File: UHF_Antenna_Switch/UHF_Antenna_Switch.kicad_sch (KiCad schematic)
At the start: 37 parts, among them J1 Conn_N_Type_Female, J2 Conn_SO-239, J3 Conn_SMA_Female, J4 Screw_Terminal_01x04, J5 Conn_02x03_Odd_Even, SW1 SW_SP3T, SW2 SW_Push, U1 LTC5507ES6, U2 PAT1220-C-10DB, U3 PCB-Trace-RF-Coupler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

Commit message: chore(pcb): Minor layout tweaks in RF area
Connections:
- net RF_PORT_TX: now reaches J2.1 (In), U3.1 (INPUT)
- net Relay_K1/RF_COMMON renamed RF_PORT_ANT
- net Relay_K1/RF_NC renamed RF_PORT_RX
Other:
- moved on the sheet: J2
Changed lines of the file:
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@@
 	)
 	(rectangle
-		(start 27.94 13.97)
+		(start 13.97 13.97)
 		(end 266.7 78.74)
 		(stroke
@@
 	(wire
 		(pts
-			(xy 54.61 45.72) (xy 62.23 45.72)
+			(xy 41.91 45.72) (xy 62.23 45.72)
 		)
 		(stroke
@@
 		)
 	)
+	(label "RF_PORT_RX"
+		(at 156.21 60.96 0)
+		(effects
+			(font
+				(size 1.27 1.27)
+			)
+			(justify left bottom)
+		)
+	)
+	(label "RF_PORT_ANT"
+		(at 222.25 64.77 0)
+		(effects
+			(font
+				(size 1.27 1.27)
+			)
+			(justify left bottom)
+		)
+	)
+	(label "RF_PORT_TX"
+		(at 43.18 45.72 0)
+		(effects
+			(font
+				(size 1.27 1.27)
+			)
+			(justify left bottom)
+		)
+	)
 	(global_label "TX_DETECTED"
 		(shape input)
@@
 	(symbol
 		(lib_id "Connector:Conn_Coaxial")
-		(at 49.53 45.72 0)
+		(at 36.83 45.72 0)
 		(mirror y)
 		(unit 1)
@@
 		(dnp no)
 		(property "Reference" "J2"
-			(at 46.99 44.7431 0)
+			(at 34.29 44.7431 0)
 			(show_name no)
 			(do_not_autoplace no)
@@
 		)
 		(property "Value" "Conn_SO-239"
-			(at 46.99 47.2831 0)
+			(at 34.29 47.2831 0)
 			(show_name no)
 			(do_not_autoplace no)
@@
 		)
 		(property "Footprint" "00-project-footprints:Amphenol N Jack 172234"
-			(at 49.53 45.72 0)
+			(at 36.83 45.72 0)
 			(hide yes)
 			(show_name no)
@@
 		)
 		(property "Datasheet" ""
-			(at 49.53 45.72 0)
+			(at 36.83 45.72 0)
 			(hide yes)
 			(show_name no)
@@
 		)
 		(property "Description" "coaxial connector (BNC, SMA, SMB, SMC, Cinch/RCA, LEMO, ...)"
-			(at 49.53 45.72 0)
+			(at 36.83 45.72 0)
 			(hide yes)
 			(show_name no)
@@
 		)
 		(property "Purpose" "TX/Uplink Input"
-			(at 39.624 49.276 0)
+			(at 26.924 49.276 0)
 			(show_name no)
 			(do_not_autoplace no)
@@
 		)
 		(property "Connector Type" "SO-239 Female"
-			(at 39.116 51.562 0)
+			(at 26.416 51.562 0)
 			(show_name no)
 			(do_not_autoplace no)
@@
 	(symbol
 		(lib_id "power:GNDS")
-		(at 49.53 50.8 0)
+		(at 36.83 50.8 0)
 		(unit 1)
 		(body_style 1)
@@
 		(dnp no)
 		(property "Reference" "#PWR04"
-			(at 49.53 57.15 0)
+			(at 36.83 57.15 0)
 			(hide yes)
 			(show_name no)
@@
 		)
 		(property "Value" "GNDS"
-			(at 49.53 54.864 0)
+			(at 36.83 54.864 0)
 			(show_name no)
 			(do_not_autoplace no)
@@
 		)
 		(property "Footprint" ""
-			(at 49.53 50.8 0)
+			(at 36.83 50.8 0)
 			(hide yes)
 			(show_name no)
@@
 		)
 		(property "Datasheet" ""
-			(at 49.53 50.8 0)
+			(at 36.83 50.8 0)
 			(hide yes)
 			(show_name no)
@@
 		)
 		(property "Description" "Power symbol creates a global label with name \"GNDS\" , signal ground"
-			(at 49.53 50.8 0)
+			(at 36.83 50.8 0)
 			(hide yes)
 			(show_name no)

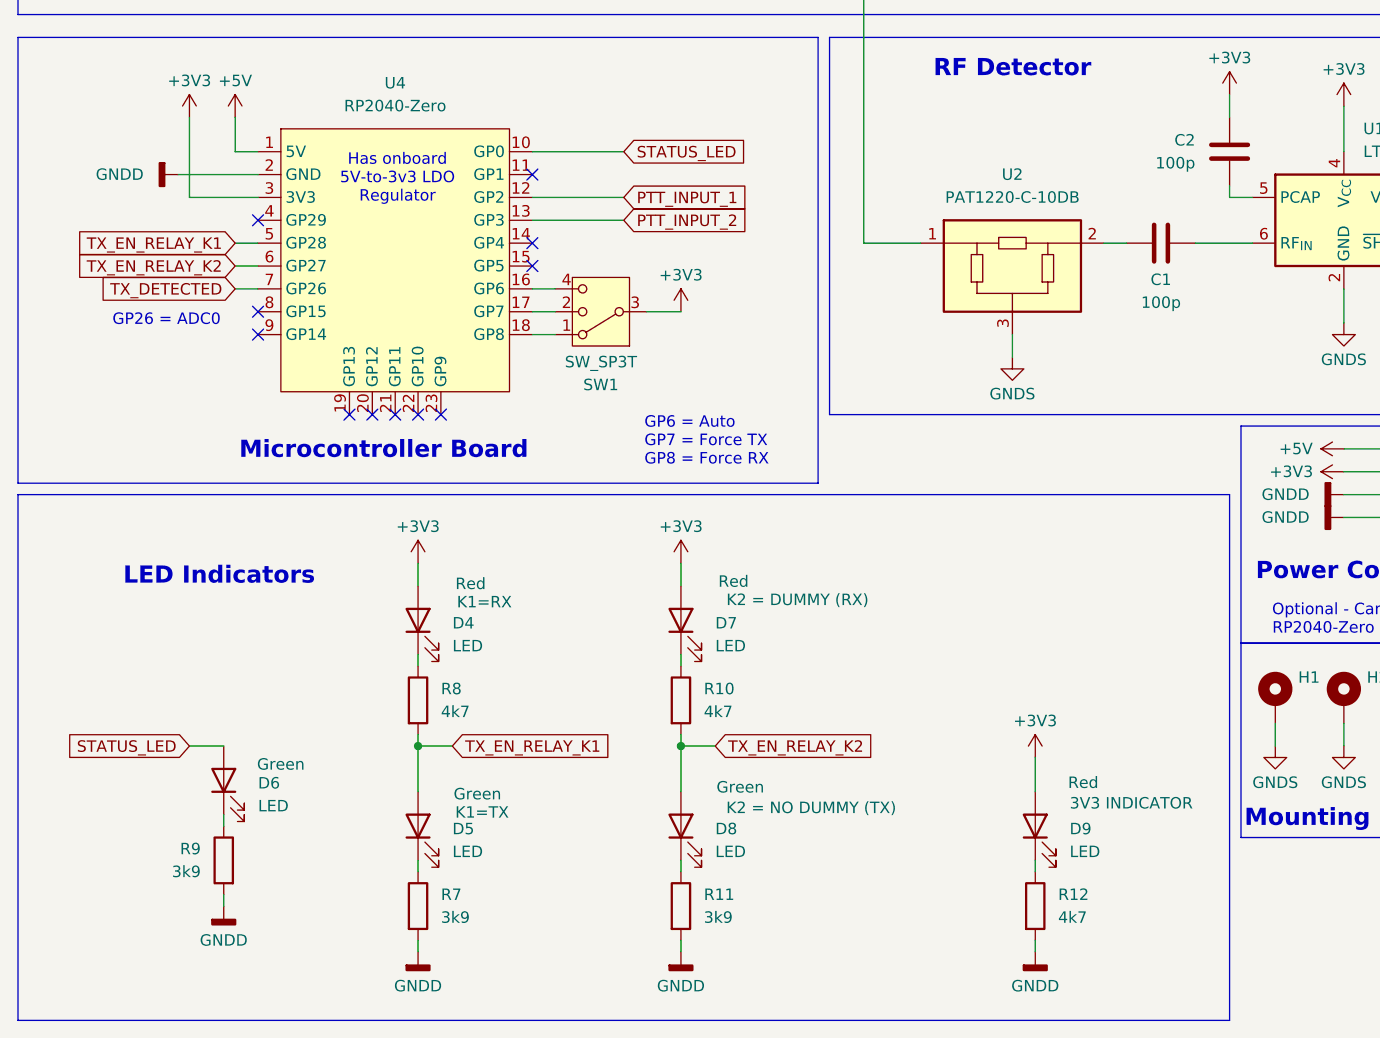
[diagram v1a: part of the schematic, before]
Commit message: feat: Add Serial Override LED indicator
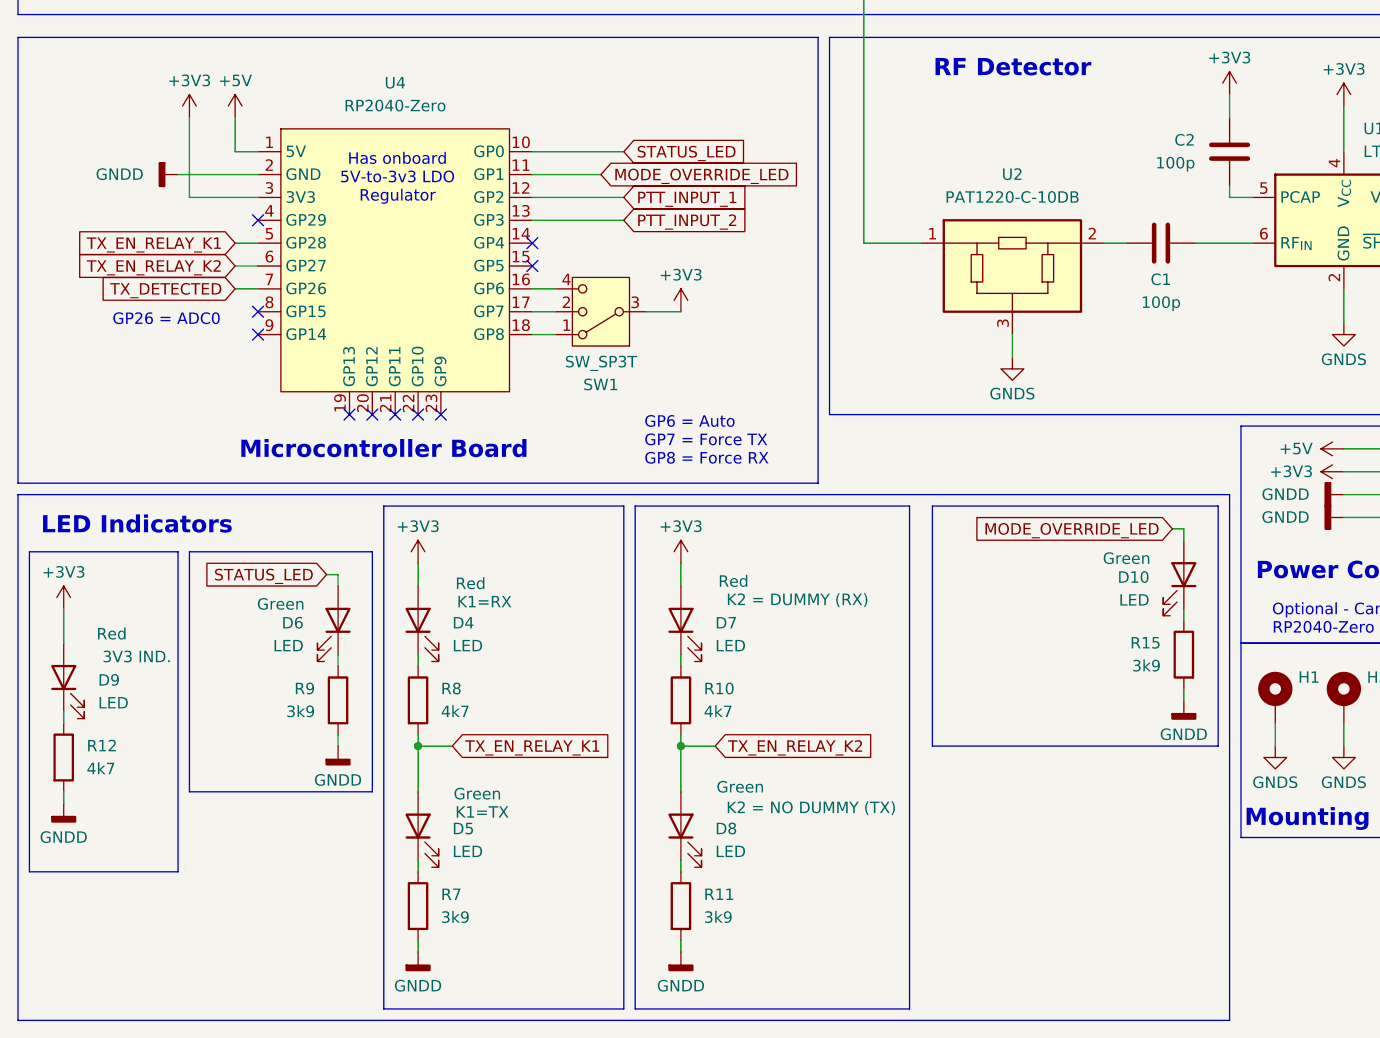
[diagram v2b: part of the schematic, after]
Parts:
- added D10: LED, LED_SMD:LED_0603_1608Metric_Pad1.05x0.95mm_HandSolder, symbol Device:LED
- added R15: 3k9, Resistor_SMD:R_0603_1608Metric_Pad0.98x0.95mm_HandSolder, symbol Device:R
- D9: Label 3V3 INDICATOR -> 3V3 IND.
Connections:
- net GNDD: now also R15.2
- net MODE_OVERRIDE_LED: now reaches U4.11 (GP1)
- net MODE_OVERRIDE_LED: now also D10.2 (A)
- new net: D10.1 (K), R15.1
- no-connect marks 11 -> 10
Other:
- moved on the sheet: D6, D9, R12, R9

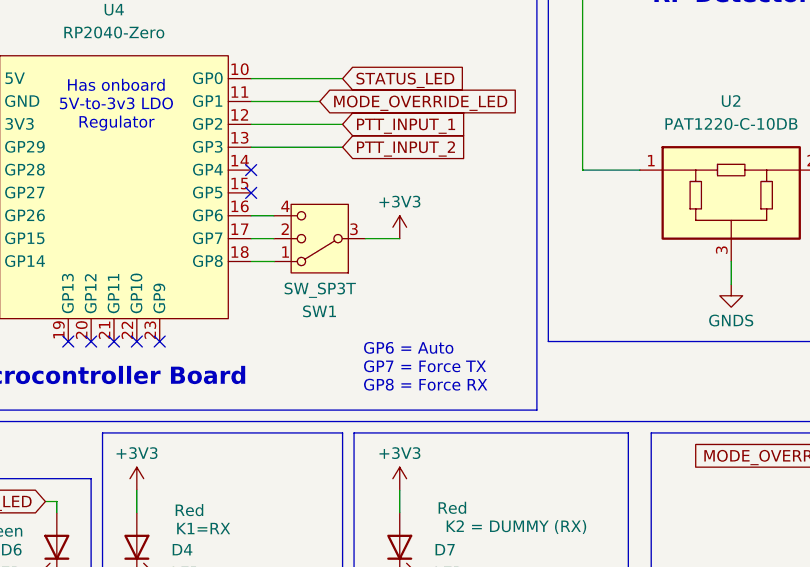
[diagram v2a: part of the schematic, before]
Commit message: fix(pcb): Swap order of mode switch items
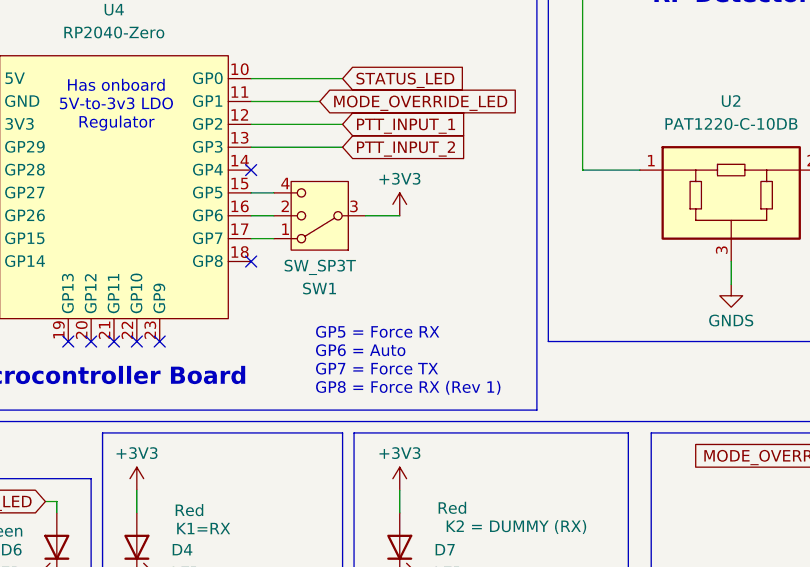
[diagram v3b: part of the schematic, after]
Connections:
- net at U4.15 (GP5): now also SW1.4
- net at U4.16 (GP6): now also SW1.2; no longer SW1.4
- net at U4.17 (GP7): now also SW1.1; no longer SW1.2
- net at U4.18 (GP8): no longer SW1.1
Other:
- note added: "GP5 = Force RX GP6 = Auto GP7 = Force TX GP8 = Force RX (Rev 1)"
- note removed: "GP6 = Auto GP7 = Force TX GP8 = Force RX"
- moved on the sheet: SW1
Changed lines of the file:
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@@
 		)
 	)
-	(text "GP6 = Auto\nGP7 = Force TX\nGP8 = Force RX"
+	(text "GP5 = Force RX\nGP6 = Auto\nGP7 = Force TX\nGP8 = Force RX (Rev 1)"
 		(exclude_from_sim no)
-		(at 83.566 126.238 0)
+		(at 78.232 125.476 0)
 		(effects
 			(font
@@
 	)
 	(no_connect
-		(at 71.12 106.68)
+		(at 50.8 123.19)
 	)
 	(no_connect
-		(at 50.8 123.19)
+		(at 71.12 114.3)
 	)
 	(no_connect
@@
 	(wire
 		(pts
-			(xy 71.12 114.3) (xy 73.66 114.3)
-		)
-		(stroke
-			(width 0)
-			(type default)
-		)
-	)
-	(wire
-		(pts
 			(xy 87.63 139.7) (xy 87.63 142.24)
 		)
@@
 	(wire
 		(pts
+			(xy 71.12 111.76) (xy 73.66 111.76)
+		)
+		(stroke
+			(width 0)
+			(type default)
+		)
+	)
+	(wire
+		(pts
 			(xy 148.59 99.06) (xy 151.13 99.06)
 		)
@@
 	(wire
 		(pts
-			(xy 205.74 133.35) (xy 205.74 139.7)
+			(xy 71.12 106.68) (xy 73.66 106.68)
 		)
 		(stroke
@@
 	(wire
 		(pts
-			(xy 127 35.56) (xy 130.81 35.56)
+			(xy 71.12 109.22) (xy 73.66 109.22)
 		)
 		(stroke
@@
 	(wire
 		(pts
-			(xy 71.12 111.76) (xy 73.66 111.76)
+			(xy 205.74 133.35) (xy 205.74 139.7)
+		)
+		(stroke
+			(width 0)
+			(type default)
+		)
+	)
+	(wire
+		(pts
+			(xy 127 35.56) (xy 130.81 35.56)
 		)
 		(stroke
@@
 	(wire
 		(pts
-			(xy 83.82 111.76) (xy 87.63 111.76)
+			(xy 83.82 109.22) (xy 87.63 109.22)
 		)
 		(stroke
@@
 	(wire
 		(pts
-			(xy 71.12 109.22) (xy 73.66 109.22)
-		)
-		(stroke
-			(width 0)
-			(type default)
-		)
-	)
-	(wire
-		(pts
 			(xy 247.65 144.78) (xy 247.65 142.24)
 		)
@@
 	(symbol
 		(lib_id "Switch:SW_SP3T")
-		(at 78.74 111.76 180)
+		(at 78.74 109.22 180)
 		(unit 1)
 		(body_style 1)
@@
 		(dnp no)
 		(property "Reference" "SW1"
-			(at 78.74 119.888 0)
+			(at 78.74 117.348 0)
 			(show_name no)
 			(do_not_autoplace no)
@@
 		)
 		(property "Value" "SW_SP3T"
-			(at 78.74 117.348 0)
+			(at 78.74 114.808 0)
 			(show_name no)
 			(do_not_autoplace no)
@@
 		)
 		(property "Footprint" "Button_Switch_SMD:SW_SP3T_PCM13"
-			(at 94.615 116.205 0)
+			(at 94.615 113.665 0)
 			(hide yes)
 			(show_name no)
@@
 		)
 		(property "Datasheet" ""
-			(at 78.74 104.14 0)
+			(at 78.74 101.6 0)
 			(hide yes)
 			(show_name no)
@@
 		)
 		(property "Description" "Switch, three position, single pole triple throw, 3 position switch, SP3T"
-			(at 78.74 111.76 0)
+			(at 78.74 109.22 0)
 			(hide yes)
 			(show_name no)
@@
 	(symbol
 		(lib_id "power:+3V3")
-		(at 87.63 111.76 0)
+		(at 87.63 109.22 0)
 		(unit 1)
 		(body_style 1)
@@
 		(dnp no)
 		(property "Reference" "#PWR027"
-			(at 87.63 115.57 0)
+			(at 87.63 113.03 0)
 			(hide yes)
 			(show_name no)
@@
 		)
 		(property "Value" "+3V3"
-			(at 87.63 107.696 0)
+			(at 87.63 105.156 0)
 			(show_name no)
 			(do_not_autoplace no)
@@
 		)
 		(property "Footprint" ""
-			(at 87.63 111.76 0)
+			(at 87.63 109.22 0)
 			(hide yes)
 			(show_name no)
@@
 		)
 		(property "Datasheet" ""
-			(at 87.63 111.76 0)
+			(at 87.63 109.22 0)
 			(hide yes)
 			(show_name no)
@@
 		)
 		(property "Description" "Power symbol creates a global label with name \"+3V3\""
-			(at 87.63 111.76 0)
+			(at 87.63 109.22 0)
 			(hide yes)
 			(show_name no)

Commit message: feat(pcb): Finish Rev 2 render, exports
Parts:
- J5, SW2: now not fitted
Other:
- note added: "PTT Interface is added as a backup option in case of non-working detector. Serial control via USB is preferred."
- note removed: "PTT Interface is added as a backup option in case of non-working detector."
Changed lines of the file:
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@@
 	(generator_version "10.0")
 	(paper "USLetter")
+	(title_block
+		(date "2026-05-30")
+		(rev "Rev 2")
+	)
 	(rectangle
 		(start 54.61 133.35)
@@
 		)
 	)
-	(text "PTT Interface is added as a backup\noption in case of non-working detector."
+	(text "PTT Interface is added as a backup\noption in case of non-working detector.\nSerial control via USB is preferred."
 		(exclude_from_sim no)
-		(at 230.632 157.48 0)
+		(at 233.426 155.956 0)
 		(effects
 			(font
@@
 		)
 	)
+	(text_box "Uplink power must be approx. >=10W to be auto-detected."
+		(exclude_from_sim no)
+		(at 21.59 58.42 0)
+		(size 39.37 5.9929)
+		(margins 0.9525 0.9525 0.9525 0.9525)
+		(stroke
+			(width 0)
+			(type solid)
+		)
+		(fill
+			(type none)
+		)
+		(effects
+			(font
+				(size 1.27 1.27)
+			)
+			(justify left top)
+		)
+	)
 	(text_box "Input to detector: -34 to 14 dBm\n\nDetector Caps (µF) ≥ 1/(30 x Freq_Min_MHz) = 1/(30 * 400) = 83 pF\nDetector Caps (µF) ≥ 1/(30 x Freq_Min_MHz) = 1/(30 * 333) = 100 pF\nUse C1=C2=100 pF (for ease of sourcing).\n"
 		(exclude_from_sim no)
@@
 	(wire
 		(pts
-			(xy 205.74 133.35) (xy 205.74 139.7)
+			(xy 205.74 134.62) (xy 205.74 139.7)
 		)
 		(stroke
@@
 	(wire
 		(pts
-			(xy 220.98 132.08) (xy 220.98 133.35)
+			(xy 220.98 132.08) (xy 220.98 134.62)
 		)
 		(stroke
@@
 	(wire
 		(pts
-			(xy 220.98 133.35) (xy 215.9 133.35)
+			(xy 220.98 134.62) (xy 215.9 134.62)
 		)
 		(stroke
@@
 		(on_board yes)
 		(in_pos_files yes)
-		(dnp no)
+		(dnp yes)
 		(property "Reference" "J5"
 			(at 237.236 134.112 0)
@@
 	(symbol
 		(lib_id "Switch:SW_Push")
-		(at 210.82 133.35 0)
+		(at 210.82 134.62 0)
 		(unit 1)
 		(body_style 1)
@@
 		(on_board yes)
 		(in_pos_files yes)
-		(dnp no)
+		(dnp yes)
 		(fields_autoplaced yes)
 		(property "Reference" "SW2"
-			(at 210.82 125.73 0)
+			(at 210.82 127 0)
 			(show_name no)
 			(do_not_autoplace no)
@@
 		)
 		(property "Value" "SW_Push"
-			(at 210.82 128.27 0)
+			(at 210.82 129.54 0)
 			(show_name no)
 			(do_not_autoplace no)
@@
 		)
 		(property "Footprint" "Button_Switch_THT:SW_PUSH_6mm_H4.3mm"
-			(at 210.82 128.27 0)
+			(at 210.82 129.54 0)
 			(hide yes)
 			(show_name no)
@@
 		)
 		(property "Datasheet" ""
-			(at 210.82 128.27 0)
+			(at 210.82 129.54 0)
 			(hide yes)
 			(show_name no)
@@
 		)
 		(property "Description" "Push button switch, generic, two pins"
-			(at 210.82 133.35 0)
+			(at 210.82 134.62 0)
 			(hide yes)
 			(show_name no)
